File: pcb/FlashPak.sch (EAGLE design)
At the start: 18 parts, among them IC1 EPROM/FLASHROM, IC2 74LS174N, IC3 74LS138N, IC4 74LS138N, X1 EXPANSION_PORT_COCO

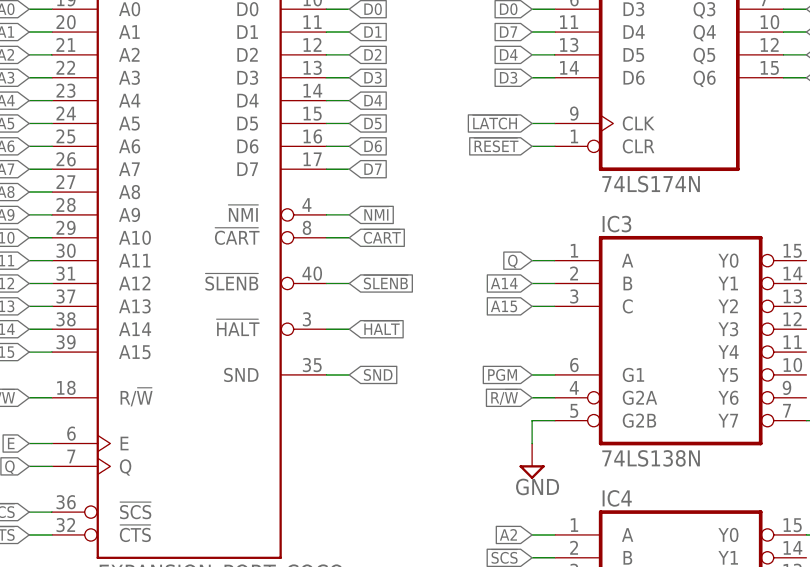
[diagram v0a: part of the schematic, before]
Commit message: Fixed issue with MPI use, added ASM, and wrote sample BASIC code
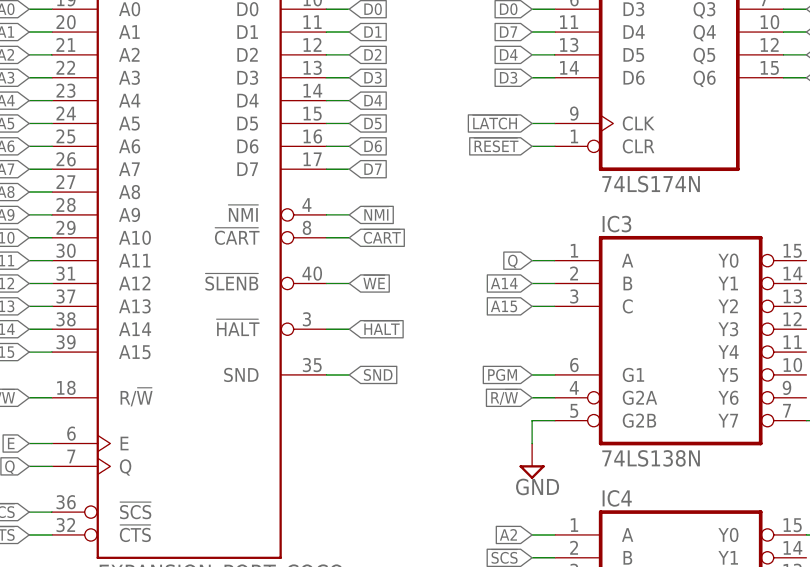
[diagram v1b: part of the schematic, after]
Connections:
- removed net !SLENB: X1X.!SLENB
- net !WE: now also X1X.!SLENB
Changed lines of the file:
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@@
 <label x="15.24" y="165.1" size="1.27" layer="95" ratio="10" rot="R180" xref="yes"/>
+</segment>
+<segment>
+<pinref part="X1" gate="X" pin="!SLENB"/>
+<wire x1="73.66" y1="170.18" x2="71.12" y2="170.18" width="0.1524" layer="91"/>
+<label x="73.66" y="170.18" size="1.27" layer="95" ratio="10" xref="yes"/>
 </segment>
 </net>
@@
 </segment>
 </net>
-<net name="!SLENB" class="0">
-<segment>
-<pinref part="X1" gate="X" pin="!SLENB"/>
-<wire x1="73.66" y1="170.18" x2="71.12" y2="170.18" width="0.1524" layer="91"/>
-<label x="73.66" y="170.18" size="1.27" layer="95" ratio="10" xref="yes"/>
-</segment>
-</net>

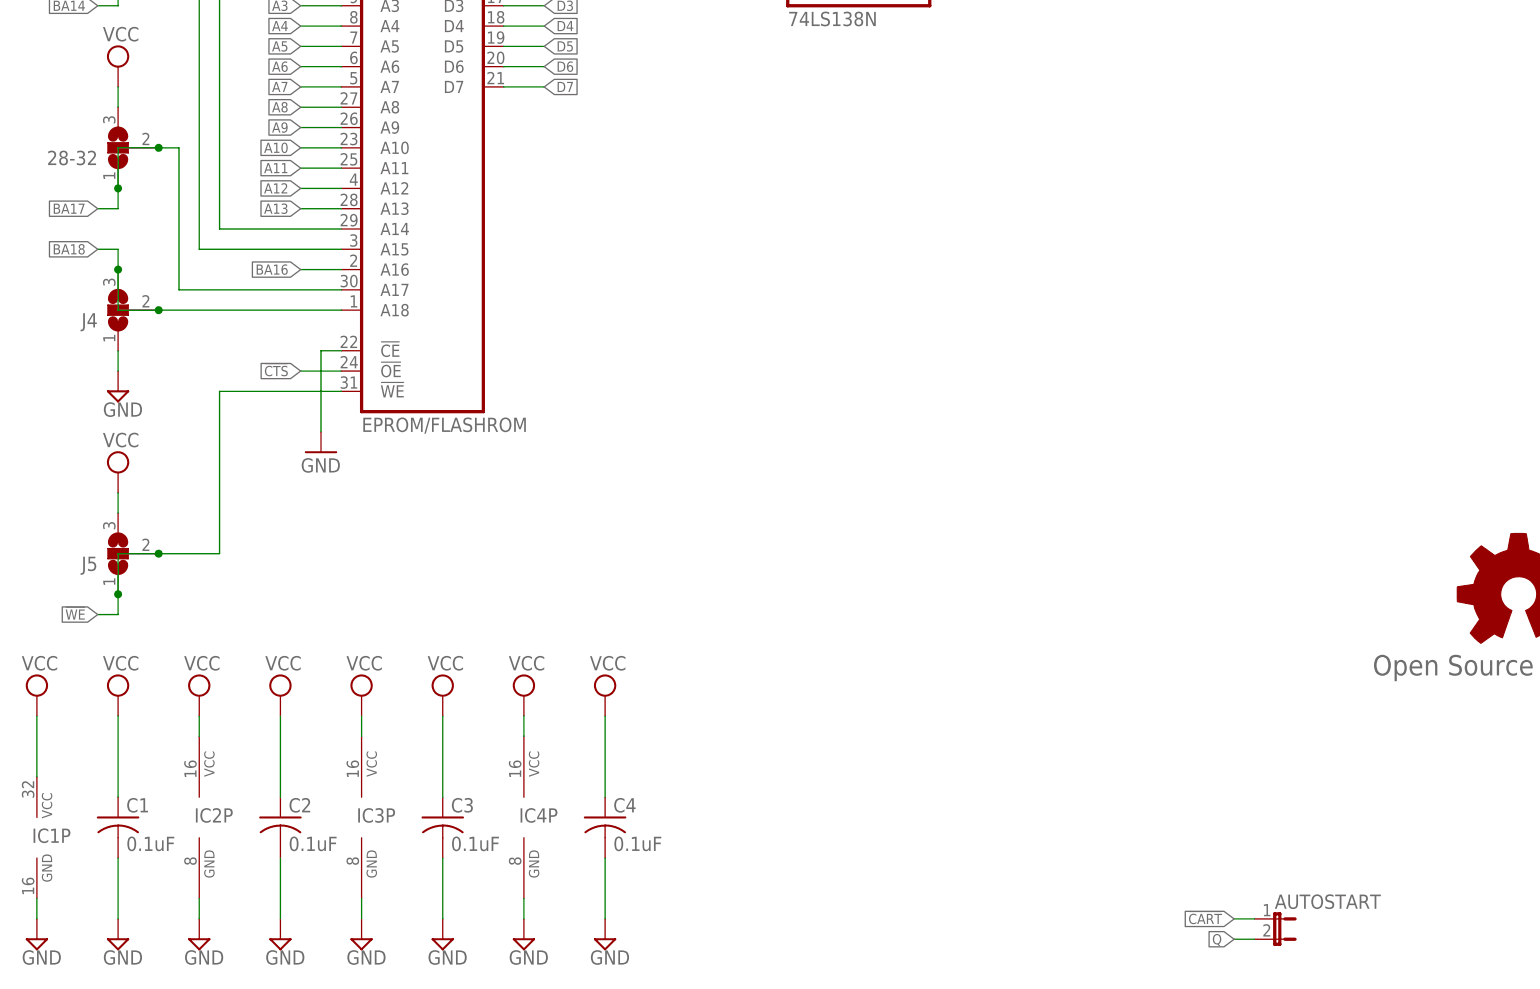
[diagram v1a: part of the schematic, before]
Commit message: Added a bit of length to the cartridge design to enable easy AUTOSTART access
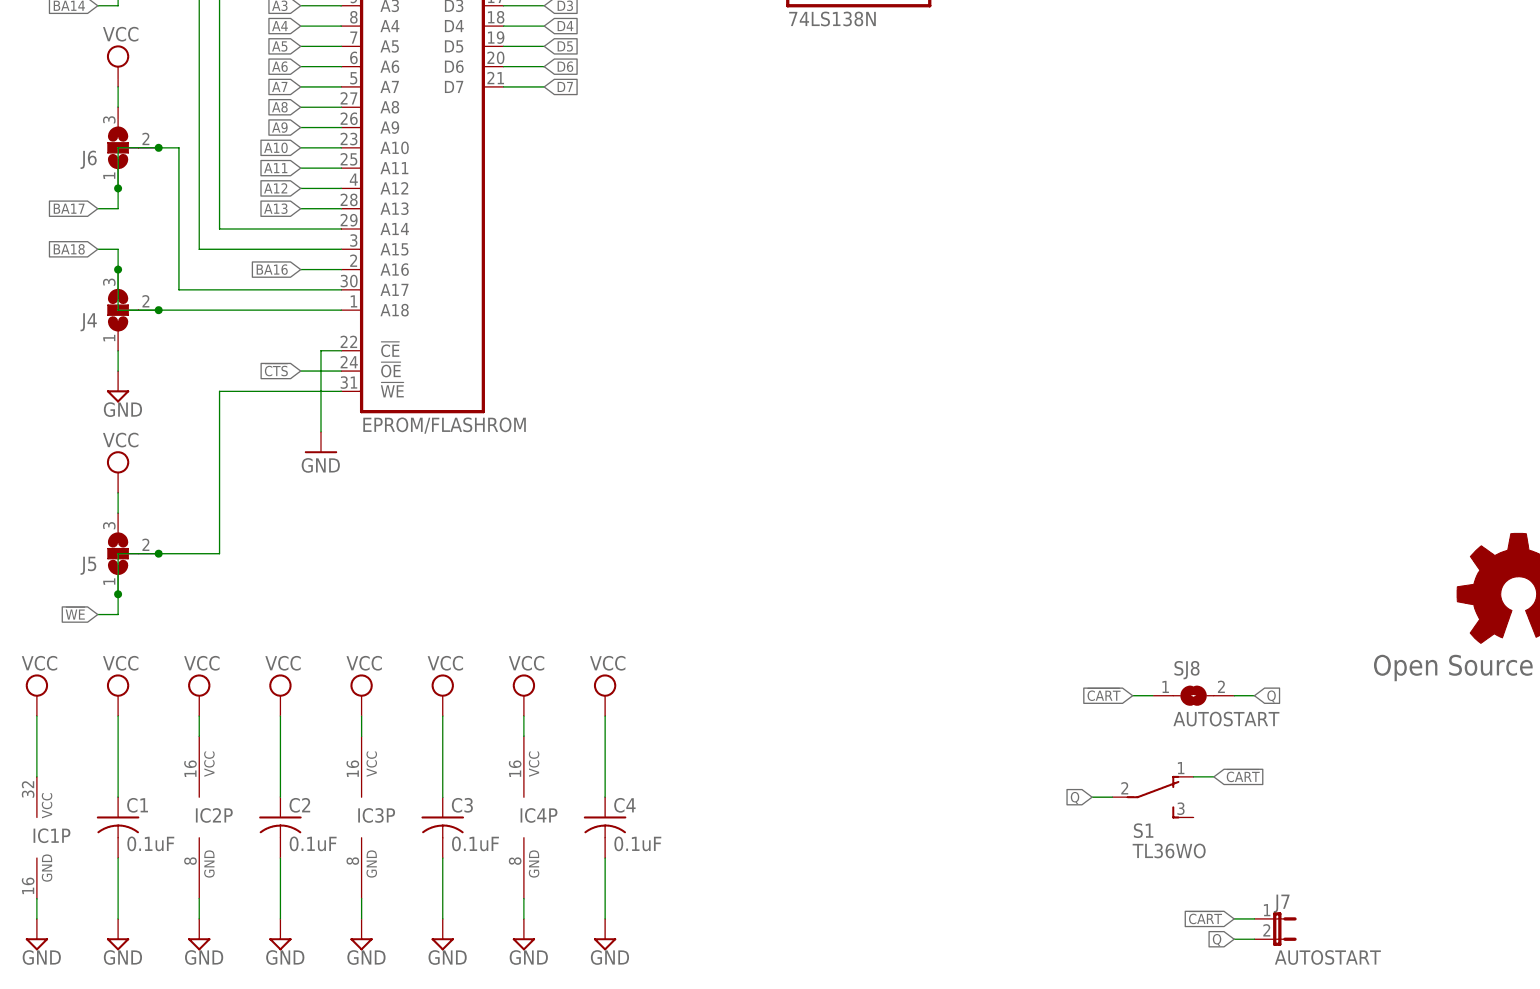
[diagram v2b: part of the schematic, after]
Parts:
- added S1: TL36WO, switch:TL36WO
- added SJ8: AUTOSTART, jumper-jlb:SJ
- J7: value (none) -> AUTOSTART
- renumbered 28-32 to J6, AUTOSTART to J7
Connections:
- net !CART: now also S1.O, SJ8.1
- net Q: now also S1.P, SJ8.2
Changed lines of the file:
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@@
 <part name="FRAME2" library="frames" deviceset="FRAME_A_L" device=""/>
 <part name="GND1" library="supply1" deviceset="GND" device=""/>
-<part name="AUTOSTART" library="jumper" deviceset="JP1E" device=""/>
+<part name="J7" library="jumper" deviceset="JP1E" device="" value="AUTOSTART"/>
 <part name="IC1" library="memory-sst" deviceset="SST39SF040A" device="PHR" value="EPROM/FLASHROM"/>
 <part name="U$1" library="coco" deviceset="PROGRAM_PAK" device=""/>
@@
 <part name="SUPPLY18" library="supply2" deviceset="GND" device=""/>
 <part name="IC3" library="74xx-us-jlb" deviceset="74*138" device="N" technology="LS"/>
-<part name="28-32" library="jumper" deviceset="SJ2W" device=""/>
+<part name="J6" library="jumper" deviceset="SJ2W" device=""/>
 <part name="SUPPLY1" library="supply2" deviceset="VCC" device=""/>
 <part name="GOLD_ORB_SM1" library="oshw" deviceset="OSHWLOGO" device="LOGO8MM" value="Open Source Hardware"/>
@@
 <part name="SUPPLY20" library="supply2" deviceset="VCC" device=""/>
 <part name="SUPPLY21" library="supply2" deviceset="GND" device=""/>
+<part name="S1" library="switch" deviceset="TL36WO" device=""/>
+<part name="SJ8" library="jumper-jlb" deviceset="SJ" device="" value="AUTOSTART"/>
 </parts>
 <sheets>
@@
 <instance part="C2" gate="G$1" x="38.1" y="20.32"/>
 <instance part="X1" gate="X" x="55.88" y="172.72"/>
-<instance part="AUTOSTART" gate="A" x="162.56" y="7.62" rot="R270"/>
+<instance part="J7" gate="A" x="162.56" y="7.62" rot="R270"/>
 <instance part="IC1" gate="A" x="55.88" y="101.6"/>
 <instance part="U$1" gate="A" x="264.16" y="45.72"/>
@@
 <instance part="IC3" gate="A" x="111.76" y="165.1"/>
 <instance part="IC3" gate="P" x="48.26" y="20.32"/>
-<instance part="28-32" gate="G$1" x="17.78" y="104.14" rot="R180"/>
+<instance part="J6" gate="G$1" x="17.78" y="104.14" rot="R180"/>
 <instance part="SUPPLY1" gate="G$1" x="17.78" y="114.3"/>
 <instance part="GOLD_ORB_SM1" gate="G$1" x="193.04" y="48.26"/>
@@
 <instance part="SUPPLY20" gate="G$1" x="68.58" y="35.56"/>
 <instance part="SUPPLY21" gate="GND" x="68.58" y="5.08"/>
+<instance part="S1" gate="BEF1" x="147.32" y="22.86" rot="R270"/>
+<instance part="SJ8" gate="1" x="152.4" y="35.56"/>
 </instances>
 <busses>
@@
 <label x="15.24" y="96.52" size="1.27" layer="95" ratio="10" rot="R180" xref="yes"/>
 <pinref part="IC1" gate="A" pin="A17"/>
-<pinref part="28-32" gate="G$1" pin="2"/>
+<pinref part="J6" gate="G$1" pin="2"/>
 <wire x1="22.86" y1="104.14" x2="25.4" y2="104.14" width="0.1524" layer="91"/>
 <wire x1="25.4" y1="104.14" x2="25.4" y2="86.36" width="0.1524" layer="91"/>
 <wire x1="25.4" y1="86.36" x2="45.72" y2="86.36" width="0.1524" layer="91"/>
 <junction x="22.86" y="104.14"/>
-<pinref part="28-32" gate="G$1" pin="1"/>
+<pinref part="J6" gate="G$1" pin="1"/>
 <wire x1="15.24" y1="96.52" x2="17.78" y2="96.52" width="0.1524" layer="91"/>
 <wire x1="17.78" y1="96.52" x2="17.78" y2="99.06" width="0.1524" layer="91"/>
@@
 <segment>
 <pinref part="SUPPLY1" gate="G$1" pin="VCC"/>
-<pinref part="28-32" gate="G$1" pin="3"/>
+<pinref part="J6" gate="G$1" pin="3"/>
 <wire x1="17.78" y1="111.76" x2="17.78" y2="109.22" width="0.1524" layer="91"/>
 </segment>
@@
 </segment>
 <segment>
-<pinref part="AUTOSTART" gate="A" pin="1"/>
+<pinref part="J7" gate="A" pin="1"/>
 <wire x1="160.02" y1="7.62" x2="157.48" y2="7.62" width="0.1524" layer="91"/>
 <label x="157.48" y="7.62" size="1.27" layer="95" ratio="10" rot="R180" xref="yes"/>
+</segment>
+<segment>
+<wire x1="152.4" y1="25.4" x2="154.94" y2="25.4" width="0.1524" layer="91"/>
+<label x="154.94" y="25.4" size="1.27" layer="95" ratio="10" xref="yes"/>
+<pinref part="S1" gate="BEF1" pin="O"/>
+</segment>
+<segment>
+<wire x1="147.32" y1="35.56" x2="144.78" y2="35.56" width="0.1524" layer="91"/>
+<label x="144.78" y="35.56" size="1.27" layer="95" ratio="10" rot="R180" xref="yes"/>
+<pinref part="SJ8" gate="1" pin="1"/>
 </segment>
 </net>
@@
 </segment>
 <segment>
-<pinref part="AUTOSTART" gate="A" pin="2"/>
+<pinref part="J7" gate="A" pin="2"/>
 <wire x1="160.02" y1="5.08" x2="157.48" y2="5.08" width="0.1524" layer="91"/>
 <label x="157.48" y="5.08" size="1.27" layer="95" ratio="10" rot="R180" xref="yes"/>
@@
 <label x="93.98" y="129.54" size="1.27" layer="95" ratio="10" rot="R180" xref="yes"/>
 </segment>
-</net>
+<segment>
+<wire x1="142.24" y1="22.86" x2="139.7" y2="22.86" width="0.1524" layer="91"/>
+<label x="139.7" y="22.86" size="1.27" layer="95" ratio="10" rot="R180" xref="yes"/>
+<pinref part="S1" gate="BEF1" pin="P"/>
+</segment>
+<segment>
+<wire x1="157.48" y1="35.56" x2="160.02" y2="35.56" width="0.1524" layer="91"/>
+<label x="160.02" y="35.56" size="1.27" layer="95" ratio="10" xref="yes"/>
+<pinref part="SJ8" gate="1" pin="2"/>
+</segment>
+</net>

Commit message: Fix bug where updating bank reg while in write mod causes race condition
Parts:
- IC4: value 74LS138N -> 74LS688N; device 74xx-us-jlb:74LS138N -> 74xx-us-jlb:74LS688N
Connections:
- net !LATCH: now also IC3A.Y0; no longer IC4A.Y0
- net !SCS: now also IC3A.G2A, IC4A.P1; no longer IC4A.B
- net !WE: now also IC4A.P=Q; no longer IC3A.Y7
- net A14: now also IC4A.Q5; no longer IC3A.B
- net A15: now also IC4A.P4; no longer IC3A.C
- net A2: now also IC3A.B; no longer IC4A.A
- net A3: now also IC3A.A; no longer IC4A.C
- net A4: now also IC3A.C; no longer IC4A.G2A
- net GND: now also IC4A.G, IC4A.P2, IC4A.P6, IC4A.P7, IC4A.Q6, IC4A.Q7; no longer IC3A.G2B
- net PGM: now also IC4A.P0; no longer IC3A.G1
- net Q: now also IC3A.G1, IC4A.P3; no longer IC3A.A, IC4A.G1
- net R/!W: now also IC3A.G2B, IC4A.Q2; no longer IC3A.G2A, IC4A.G2B
- net VCC: now also IC4A.P5, IC4A.Q0, IC4A.Q1, IC4A.Q3, IC4A.Q4
